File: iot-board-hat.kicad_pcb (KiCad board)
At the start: 2 copper layers, 45 x 45 mm, 12 parts, among them J1 Conn_02x14_Odd_Even, J2 Conn_02x04_Counter_Clockwise, J3 Conn_01x04, J4 67298-3090, J5 Screw_Terminal_01x02, J6 USB_B_Micro, J7 Conn_02x14_Odd_Even, J8 FC68127

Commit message: some tweaks
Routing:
- net GND: track 188.0 -> 178.6 mm, vias 1 -> 0
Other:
- board size 45 x 45 mm -> 45 x 45.2 mm
- board text added: "IoT Pi IO board"
- board text added: "github.com/buxtronix/iot-pi-hat"

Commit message: Various updates/tweaks
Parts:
- moved J2 0.25 mm to (112.5, 100.6)
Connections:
- net Net-(J3-Pad1) renamed /c-vid
- net Net-(J3-Pad3) renamed /a-r
- net Net-(J3-Pad4) renamed /a-l
- J1 pad 25: /a25 -> GND
- J1 pad 9: /a9 -> GND
- J7 pad 25: /a25 -> GND
- J7 pad 9: /a9 -> GND
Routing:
- net GND: track 178.6 -> 221.1 mm
- net +5V: track 84.0 -> 75.3 mm
- net /a9: track 7.58 -> 0.00 mm
- net /a25: track 7.58 -> 0.00 mm
- removed copper zone on B.Cu, net +5V
- removed copper zone on F.Cu, net GND
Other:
- board text added: "Exp"
- board text added: "G"
- board text added: "I/O board for VK2BV IoT Pi"
- board text added: "L"
- board text added: "Pi"
- board text added: "Pwr In"
- board text added: "R"
- board text added: "V"
- board text removed: "IoT Pi IO board"

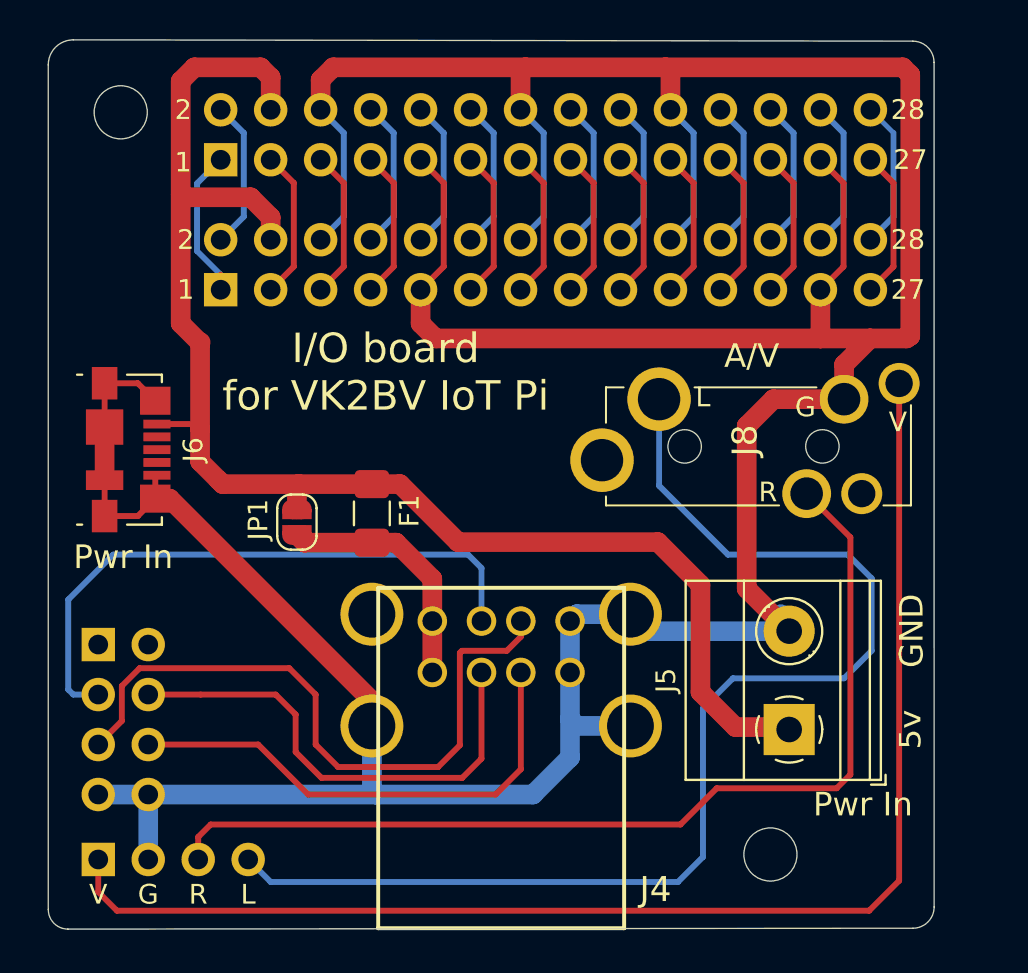
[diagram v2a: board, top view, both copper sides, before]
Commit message: Version with alternate USB ports
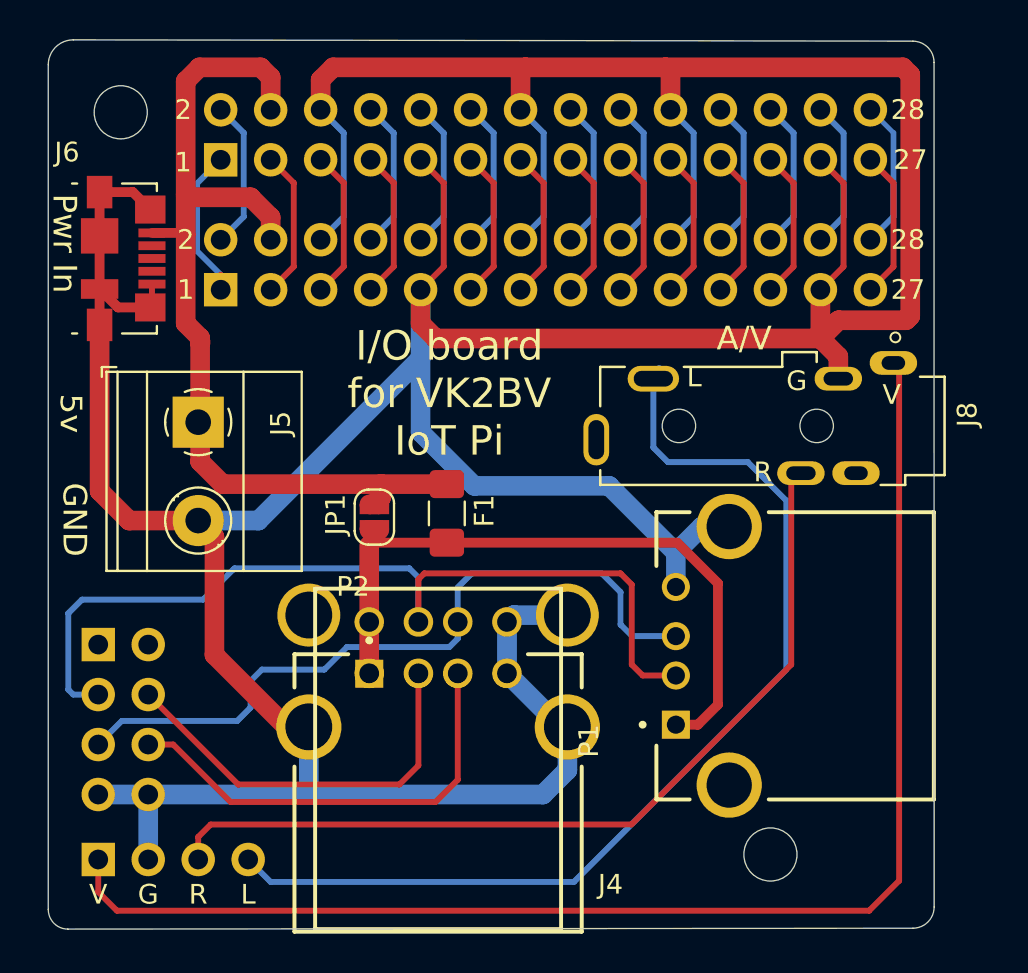
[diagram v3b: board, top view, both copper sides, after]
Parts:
- added P1: 87520-0010BLF, iot-board-hat:SAMTEC_USB-A-S-X-X-TH, F.Cu at (144.6, 101.2)
- added P2: 87520-0010BLF, iot-board-hat:SAMTEC_USB-A-S-X-X-TH, F.Cu at (129.8, 104.8)
- J8: footprint iot-board-hat:FC68127 -> SnapEDA Library:CLIFF_FC68127
- moved J5 33.9 mm to (117.6, 89.3), turned to 270 degrees
- moved J6 9.72 mm to (113.8, 81.0)
- moved J8 4.71 mm to (149.0, 89.5)
- moved JP1 3.95 mm to (126.6, 94.1)
- moved F1 3.81 mm to (130.2, 93.9)
- moved J4 3.21 mm to (129.8, 102.0)
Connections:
- net Net-(F1-Pad1) renamed +5F
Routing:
- net +5V: track 75.3 -> 48.5 mm
- net GND: track 221.1 -> 245.0 mm
- net +5F: track 12.6 -> 34.4 mm
- net USB2-: track 31.4 -> 46.9 mm
- net /a-l: track 62.3 -> 52.5 mm
- net /a-r: track 50.8 -> 44.8 mm
- net USB1-: track 24.5 -> 20.7 mm
- net USB2+: track 34.0 -> 37.6 mm
- net USB1+: track 25.2 -> 22.8 mm
- net /c-vid: track 68.7 -> 69.8 mm

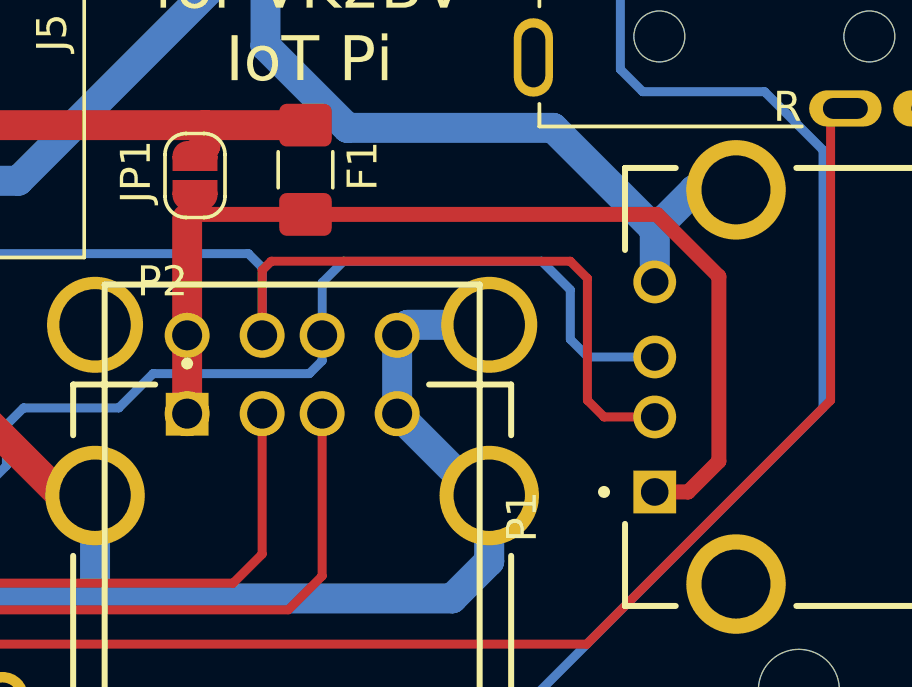
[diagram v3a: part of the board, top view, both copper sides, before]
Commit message: fix power line
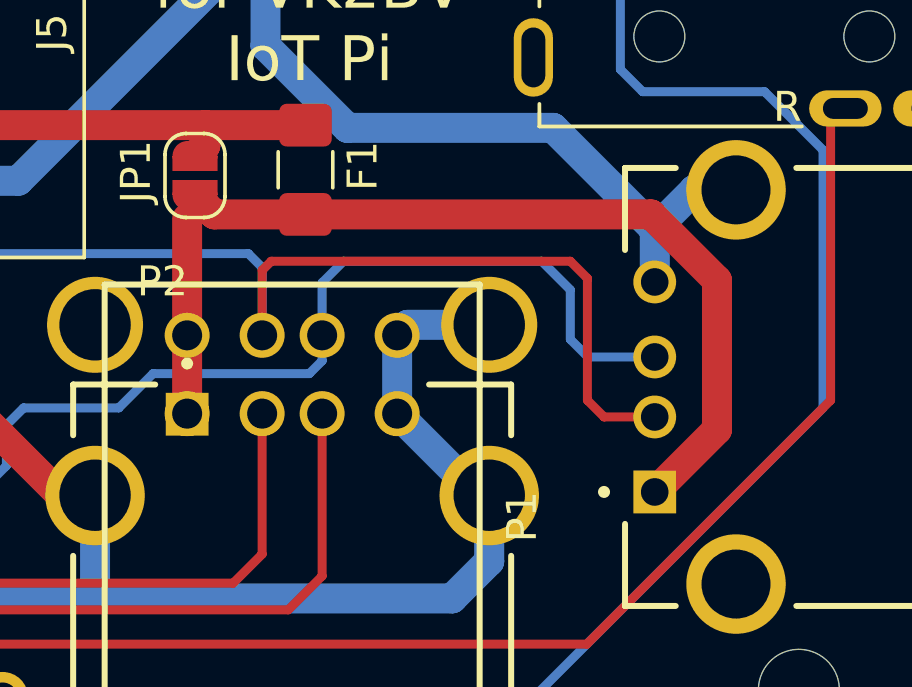
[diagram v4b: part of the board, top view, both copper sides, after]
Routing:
- net +5F: track 34.4 -> 33.7 mm
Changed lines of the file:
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@@
     (thickness 1.6)
     (drawings 32)
-    (tracks 242)
+    (tracks 243)
     (zones 0)
     (modules 14)
@@
   (segment (start 122.081 104.7645) (end 118.4275 101.111) (width 1) (layer F.Cu) (net 1))
   (segment (start 118.4275 95.1065) (end 117.602 94.281) (width 1) (layer F.Cu) (net 1))
-  (segment (start 118.4275 101.111) (end 118.4275 95.1065) (width 1) (layer F.Cu) (net 1))
   (segment (start 120.6665 94.281) (end 128.905 86.0425) (width 1) (layer B.Cu) (net 1))
   (segment (start 117.602 94.281) (end 120.6665 94.281) (width 1) (layer B.Cu) (net 1))
@@
   (segment (start 143.1995 94.5855) (end 141.8795 95.9055) (width 1) (layer B.Cu) (net 1))
   (segment (start 144.5895 94.5855) (end 143.1995 94.5855) (width 1) (layer B.Cu) (net 1))
+  (segment (start 118.4275 101.111) (end 118.4275 95.1065) (width 1) (layer F.Cu) (net 1))
   (segment (start 121.285 71.755) (end 121.285 73.406) (width 1) (layer F.Cu) (net 2))
   (segment (start 120.777 71.247) (end 121.285 71.755) (width 1) (layer F.Cu) (net 2))
@@
   (segment (start 136.694158 112.649) (end 147.489158 101.854) (width 0.3) (layer B.Cu) (net 31))
   (segment (start 120.142 111.506) (end 121.285 112.649) (width 0.3) (layer B.Cu) (net 31))
-  (segment (start 126.4285 95.404) (end 141.9495 95.404) (width 0.5) (layer F.Cu) (net 32))
-  (segment (start 141.9495 95.404) (end 144.018 97.4725) (width 0.5) (layer F.Cu) (net 32))
-  (segment (start 144.018 97.4725) (end 144.018 103.632) (width 0.5) (layer F.Cu) (net 32))
-  (segment (start 142.9945 104.6555) (end 141.8795 104.6555) (width 0.5) (layer F.Cu) (net 32))
-  (segment (start 144.018 103.632) (end 142.9945 104.6555) (width 0.5) (layer F.Cu) (net 32))
   (segment (start 126.294 102.0445) (end 126.294 99.4345) (width 1) (layer F.Cu) (net 32))
   (segment (start 126.294 99.4345) (end 126.294 95.5385) (width 1) (layer F.Cu) (net 32))
   (segment (start 126.4285 94.884) (end 126.5555 94.757) (width 0.3) (layer F.Cu) (net 32))
   (segment (start 126.4285 95.404) (end 126.4285 94.884) (width 0.3) (layer F.Cu) (net 32))
+  (segment (start 141.8795 104.6555) (end 143.9545 102.5805) (width 1) (layer F.Cu) (net 32))
+  (segment (start 143.9545 102.5805) (end 143.9545 97.5995) (width 1) (layer F.Cu) (net 32))
+  (segment (start 141.759 95.404) (end 130.2385 95.404) (width 1) (layer F.Cu) (net 32))
+  (segment (start 143.9545 97.5995) (end 141.759 95.404) (width 1) (layer F.Cu) (net 32))
+  (segment (start 127.2025 95.404) (end 126.5555 94.757) (width 1) (layer F.Cu) (net 32))
+  (segment (start 130.2385 95.404) (end 127.2025 95.404) (width 1) (layer F.Cu) (net 32))
 )
